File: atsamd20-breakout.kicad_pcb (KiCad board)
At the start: 2 copper layers, 24 x 50 mm, 34 parts, among them J1 SWD, J2 Left, J3 Right, Q1 BC847, SW1 Reset, U1 ATSAMD20E18A-A, Y1 32.768kHz, Y2 8MHz

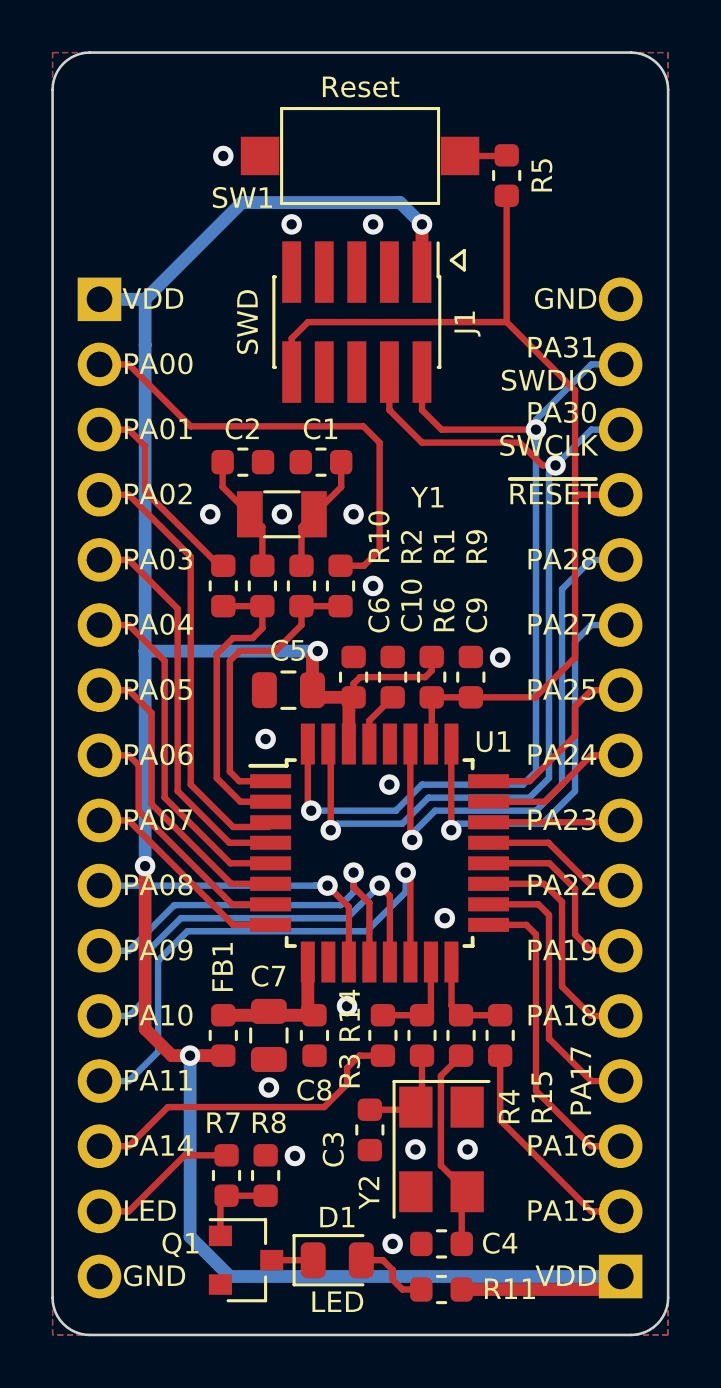
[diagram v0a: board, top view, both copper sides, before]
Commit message: Project upgrade to KiCad 6
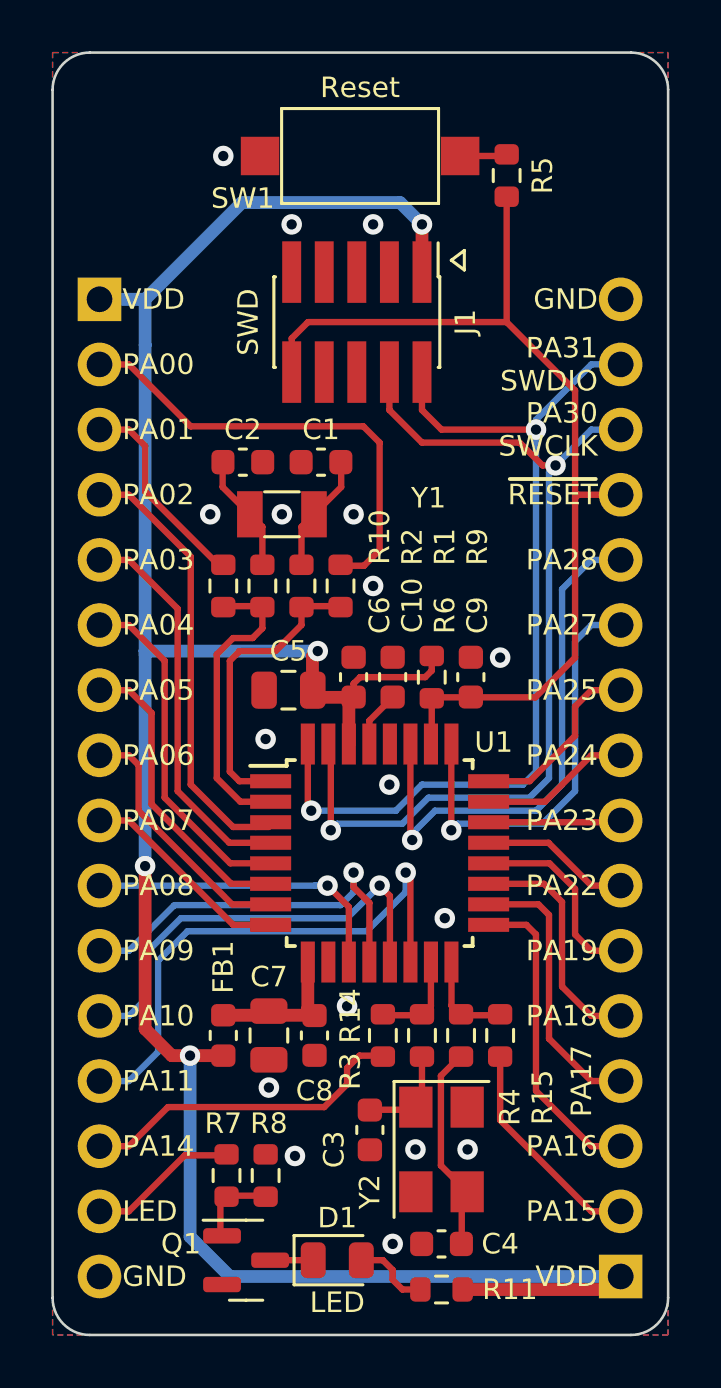
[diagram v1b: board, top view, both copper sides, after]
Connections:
- net /~RESET renamed /~{RESET}
- J1 pad 6: Net-(J1-Pad6) -> unconnected-(J1-Pad6)
- J1 pad 7: Net-(J1-Pad7) -> unconnected-(J1-Pad7)
- J1 pad 8: Net-(J1-Pad8) -> unconnected-(J1-Pad8)
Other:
- net class Default removed
- net class Power removed
- board text added: "~{RESET}"
- board text removed: "~RESET"
